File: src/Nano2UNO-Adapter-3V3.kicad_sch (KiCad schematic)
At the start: 13 parts, among them J1 ESW-108-33-L-S, J2 ESW-110-33-L-S, J3 ESW-108-33-L-S, J4 ESW-106-33-L-S, J5 PPPC151LFBN-RC, J6 PPPC151LFBN-RC, J7 TSW-103-15-L-D, J8 PJ-102A, SW1 1825910-6, U1 R-78K5.0-0.5

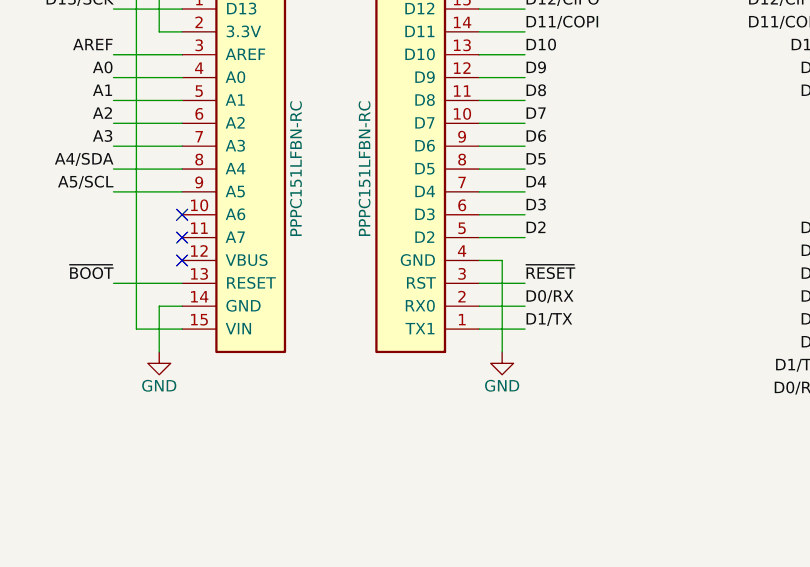
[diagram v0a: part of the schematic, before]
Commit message: Added additional part metadata to the schematic. Changed RST to RESET on one of the schematic symbols. Changed the revision from 1.0.0 to 1.0.1.
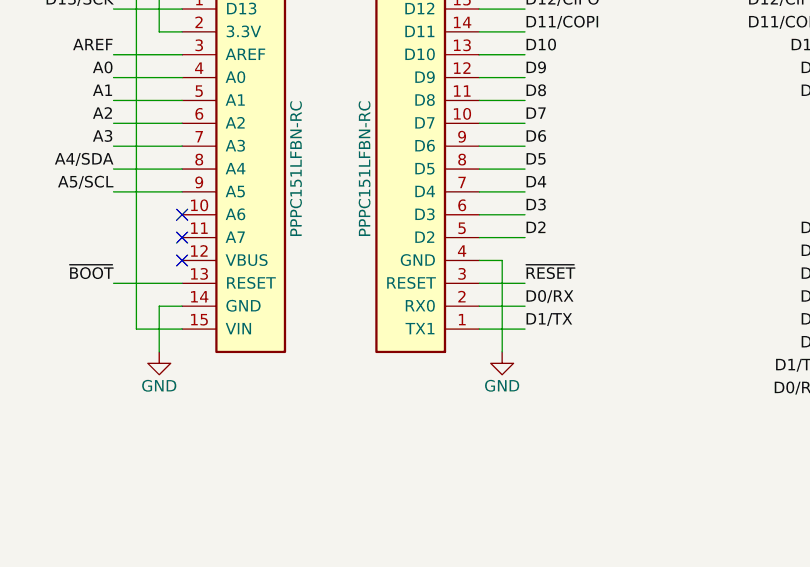
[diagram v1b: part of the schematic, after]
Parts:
- C1, C2: Manufacturer (none) -> Panasonic; Part Number (none) -> ECE-A1HKS100
- D1: Manufacturer (none) -> Vishay; Part Number (none) -> SB260S-E3/54
- J1, J3: Manufacturer (none) -> Samtec; Part Number (none) -> ESW-108-33-L-S
- J2: Manufacturer (none) -> Samtec; Part Number (none) -> ESW-110-33-L-S
- J4: Manufacturer (none) -> Samtec; Part Number (none) -> ESW-106-33-L-S
- J5, J6: Manufacturer (none) -> Sullins; Part Number (none) -> PPPC151LFBN-RC
- J7: Manufacturer (none) -> TSW/Samtec; Part Number (none) -> TSW-103-15-L-D
- J8: Manufacturer (none) -> CUI; Part Number (none) -> PJ-102A
- SW1: Manufacturer (none) -> TE; Part Number (none) -> 1825910-6
- U1: Manufacturer (none) -> RECOM; Part Number (none) -> R-78K5.0-0.5
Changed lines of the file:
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@@
   (title_block
     (title "Nano2UNO Adapter 3V3")
-    (date "2023-12-16")
-    (rev "1.0.0")
+    (date "2023-12-31")
+    (rev "1.0.1")
     (company "Designer: C. M. Bulliner")
     (comment 2 "OF MERCHANTABILITY, SATISFACTORY QUALITY AND FITNESS FOR A PARTICULAR PURPOSE.")
@@
     )
     (property "Datasheet" "https://suddendocs.samtec.com/catalog_english/esq_th.pdf" (at 68.58 63.5 0)
+      (effects (font (size 1.27 1.27)) hide)
+    )
+    (property "Description" "1x8 Socket Header" (at 68.58 45.72 0)
+      (effects (font (size 1.27 1.27)) hide)
+    )
+    (property "Manufacturer" "Samtec" (at 68.58 45.72 0)
+      (effects (font (size 1.27 1.27)) hide)
+    )
+    (property "Part Number" "ESW-108-33-L-S" (at 68.58 45.72 0)
       (effects (font (size 1.27 1.27)) hide)
     )
@@
     )
     (property "Datasheet" "https://suddendocs.samtec.com/catalog_english/esq_th.pdf" (at 210.82 30.48 0)
+      (effects (font (size 1.27 1.27)) hide)
+    )
+    (property "Description" "1x10 Socket Header" (at 210.82 50.8 0)
+      (effects (font (size 1.27 1.27)) hide)
+    )
+    (property "Manufacturer" "Samtec" (at 210.82 50.8 0)
+      (effects (font (size 1.27 1.27)) hide)
+    )
+    (property "Part Number" "ESW-110-33-L-S" (at 210.82 50.8 0)
       (effects (font (size 1.27 1.27)) hide)
     )
@@
       (effects (font (size 1.27 1.27)) hide)
     )
+    (property "Description" "1x6 Socket Header" (at 68.58 81.28 0)
+      (effects (font (size 1.27 1.27)) hide)
+    )
+    (property "Manufacturer" "Samtec" (at 68.58 81.28 0)
+      (effects (font (size 1.27 1.27)) hide)
+    )
+    (property "Part Number" "ESW-106-33-L-S" (at 68.58 81.28 0)
+      (effects (font (size 1.27 1.27)) hide)
+    )
     (pin "1")
     (pin "2")
@@
     )
     (property "Datasheet" "https://suddendocs.samtec.com/catalog_english/esq_th.pdf" (at 210.82 69.85 0)
+      (effects (font (size 1.27 1.27)) hide)
+    )
+    (property "Description" "1x8 Socket Header" (at 210.82 86.36 0)
+      (effects (font (size 1.27 1.27)) hide)
+    )
+    (property "Manufacturer" "Samtec" (at 210.82 86.36 0)
+      (effects (font (size 1.27 1.27)) hide)
+    )
+    (property "Part Number" "ESW-108-33-L-S" (at 210.82 86.36 0)
       (effects (font (size 1.27 1.27)) hide)
     )
@@
       (effects (font (size 1.27 1.27)) hide)
     )
+    (property "Description" "DO-41 Diode" (at 78.74 139.7 0)
+      (effects (font (size 1.27 1.27)) hide)
+    )
+    (property "Manufacturer" "Vishay" (at 78.74 139.7 0)
+      (effects (font (size 1.27 1.27)) hide)
+    )
+    (property "Part Number" "SB260S-E3/54" (at 78.74 139.7 0)
+      (effects (font (size 1.27 1.27)) hide)
+    )
     (pin "1")
     (pin "2")
@@
     )
     (property "Datasheet" "https://suddendocs.samtec.com/catalog_english/tsw_th.pdf" (at 173.355 146.05 0)
+      (effects (font (size 1.27 1.27)) hide)
+    )
+    (property "Description" "2x3 Pin Header" (at 205.74 132.08 0)
+      (effects (font (size 1.27 1.27)) hide)
+    )
+    (property "Manufacturer" "TSW/Samtec" (at 205.74 132.08 0)
+      (effects (font (size 1.27 1.27)) hide)
+    )
+    (property "Part Number" "TSW-103-15-L-D" (at 205.74 132.08 0)
       (effects (font (size 1.27 1.27)) hide)
     )
@@
       (effects (font (size 1.27 1.27)) hide)
     )
+    (property "Description" "10uF X7R Through-Hole Capacitor" (at 114.3 146.05 0)
+      (effects (font (size 1.27 1.27)) hide)
+    )
+    (property "Manufacturer" "Panasonic" (at 114.3 146.05 0)
+      (effects (font (size 1.27 1.27)) hide)
+    )
+    (property "Part Number" "ECE-A1HKS100 " (at 114.3 146.05 0)
+      (effects (font (size 1.27 1.27)) hide)
+    )
     (pin "1")
     (pin "2")
@@
     )
     (property "Datasheet" "https://drawings-pdf.s3.amazonaws.com/10492.pdf" (at 134.62 90.17 0)
+      (effects (font (size 1.27 1.27)) hide)
+    )
+    (property "Description" "1x15 Socket Header" (at 134.62 68.58 0)
+      (effects (font (size 1.27 1.27)) hide)
+    )
+    (property "Manufacturer" "Sullins" (at 134.62 68.58 0)
+      (effects (font (size 1.27 1.27)) hide)
+    )
+    (property "Part Number" "PPPC151LFBN-RC" (at 134.62 68.58 0)
       (effects (font (size 1.27 1.27)) hide)
     )
@@
     )
   )
-  (symbol (lib_name "Conn_01x15_1") (lib_id "Project_Symbols:Conn_01x15_Nano_1") (at 157.48 68.58 180) (unit 1)
+  (symbol (lib_id "Project_Symbols:Conn_01x15_Nano_1") (at 157.48 68.58 180) (unit 1)
     (in_bom yes) (on_board yes) (dnp no)
     (property "Reference" "J5" (at 154.94 46.99 0)
@@
     )
     (property "Datasheet" "https://drawings-pdf.s3.amazonaws.com/10492.pdf" (at 157.48 44.45 0)
+      (effects (font (size 1.27 1.27)) hide)
+    )
+    (property "Description" "1x15 Socket Header" (at 157.48 68.58 0)
+      (effects (font (size 1.27 1.27)) hide)
+    )
+    (property "Manufacturer" "Sullins" (at 157.48 68.58 0)
+      (effects (font (size 1.27 1.27)) hide)
+    )
+    (property "Part Number" "PPPC151LFBN-RC" (at 157.48 68.58 0)
       (effects (font (size 1.27 1.27)) hide)
     )
@@
       (effects (font (size 1.27 1.27)) hide)
     )
+    (property "Description" "6mm Pushbutton Switch" (at 88.9 50.8 0)
+      (effects (font (size 1.27 1.27)) hide)
+    )
+    (property "Manufacturer" "TE" (at 88.9 50.8 0)
+      (effects (font (size 1.27 1.27)) hide)
+    )
+    (property "Part Number" "1825910-6" (at 88.9 50.8 0)
+      (effects (font (size 1.27 1.27)) hide)
+    )
     (pin "1")
     (pin "2")
@@
       (effects (font (size 1.27 1.27)) hide)
     )
+    (property "Description" "5V DC DC Converter" (at 101.6 139.7 0)
+      (effects (font (size 1.27 1.27)) hide)
+    )
+    (property "Manufacturer" "RECOM" (at 101.6 139.7 0)
+      (effects (font (size 1.27 1.27)) hide)
+    )
+    (property "Part Number" "R-78K5.0-0.5" (at 101.6 139.7 0)
+      (effects (font (size 1.27 1.27)) hide)
+    )
     (pin "1")
     (pin "2")
@@
       (effects (font (size 1.27 1.27)) hide)
     )
+    (property "Description" "10uF X7R Through-Hole Capacitor" (at 88.9 146.05 0)
+      (effects (font (size 1.27 1.27)) hide)
+    )
+    (property "Manufacturer" "Panasonic" (at 88.9 146.05 0)
+      (effects (font (size 1.27 1.27)) hide)
+    )
+    (property "Part Number" "ECE-A1HKS100 " (at 88.9 146.05 0)
+      (effects (font (size 1.27 1.27)) hide)
+    )
     (pin "1")
     (pin "2")
@@
       (effects (font (size 1.27 1.27)) hide)
     )
+    (property "Description" "2.0mm ID, 5.5mm OD Barrel Jack" (at 53.34 142.24 0)
+      (effects (font (size 1.27 1.27)) hide)
+    )
+    (property "Manufacturer" "CUI" (at 53.34 142.24 0)
+      (effects (font (size 1.27 1.27)) hide)
+    )
+    (property "Part Number" "PJ-102A" (at 53.34 142.24 0)
+      (effects (font (size 1.27 1.27)) hide)
+    )
